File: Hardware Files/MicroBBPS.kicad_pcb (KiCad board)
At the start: 2 copper layers, 54 x 100 mm, 24 parts, among them J1 Conn_01x06, J2 USB_B_Micro, J3 Conn_02x03_Counter_Clockwise, J4 Conn_02x03_Counter_Clockwise, J5 Conn_01x02, J8 3PoleHeaderSwitch, J9 3PoleHeaderSwitch, U1 NCP1117ST50T3G, U3 NCP1117ST33T3G

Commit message: Update routing to match main
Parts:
- removed J1: Conn_01x06, MicroBBPS:Breadboard_Row_25
- removed REF** (x2): MountingHole_3.2mm_M3_ISO7380, MountingHole:MountingHole_3.2mm_M3_ISO7380
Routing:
- net /VoutRight: track 78.2 -> 0.00 mm
- net /VoutLeft: track 75.1 -> 0.00 mm
- net VS: track 42.7 -> 53.7 mm, vias 1 -> 3
- net GND: vias 0 -> 4
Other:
- board size 54 x 100 mm -> 54 x 23 mm

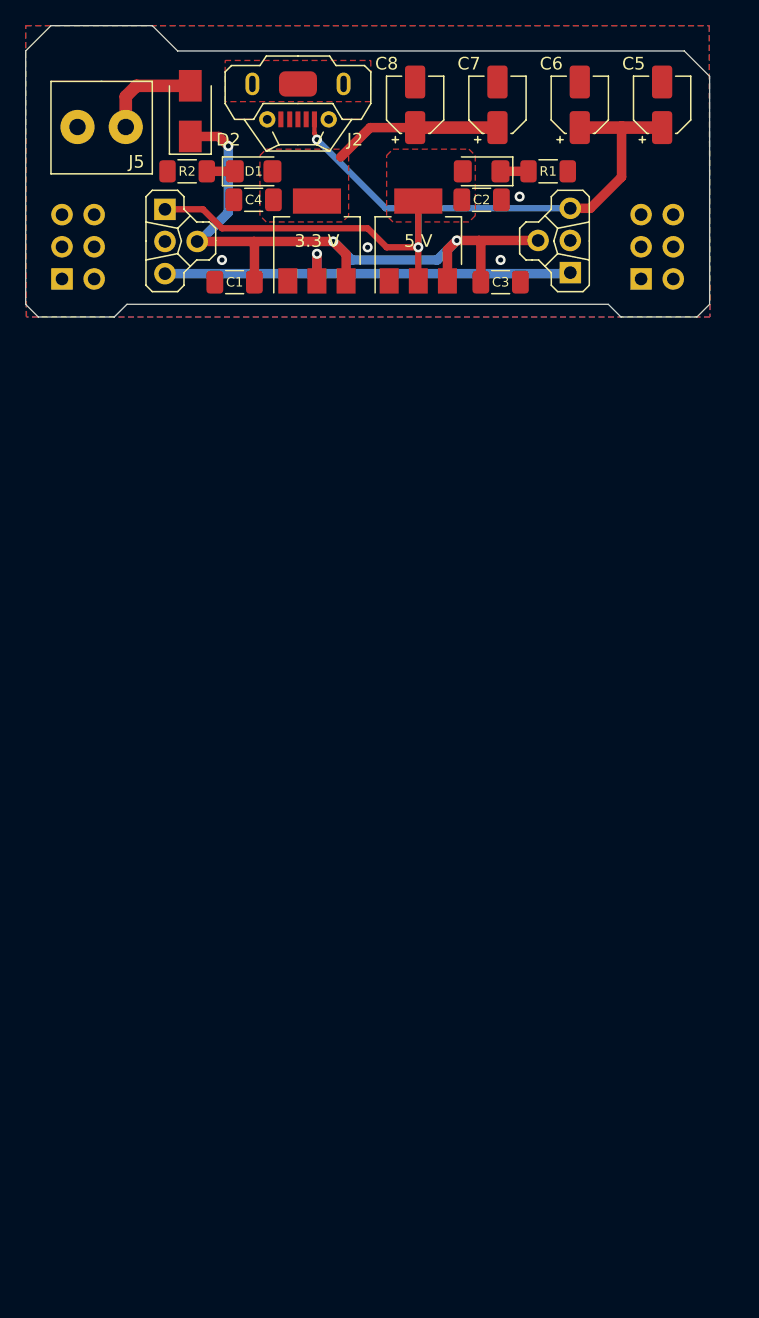
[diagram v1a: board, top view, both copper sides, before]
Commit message: Fix board version mismatch
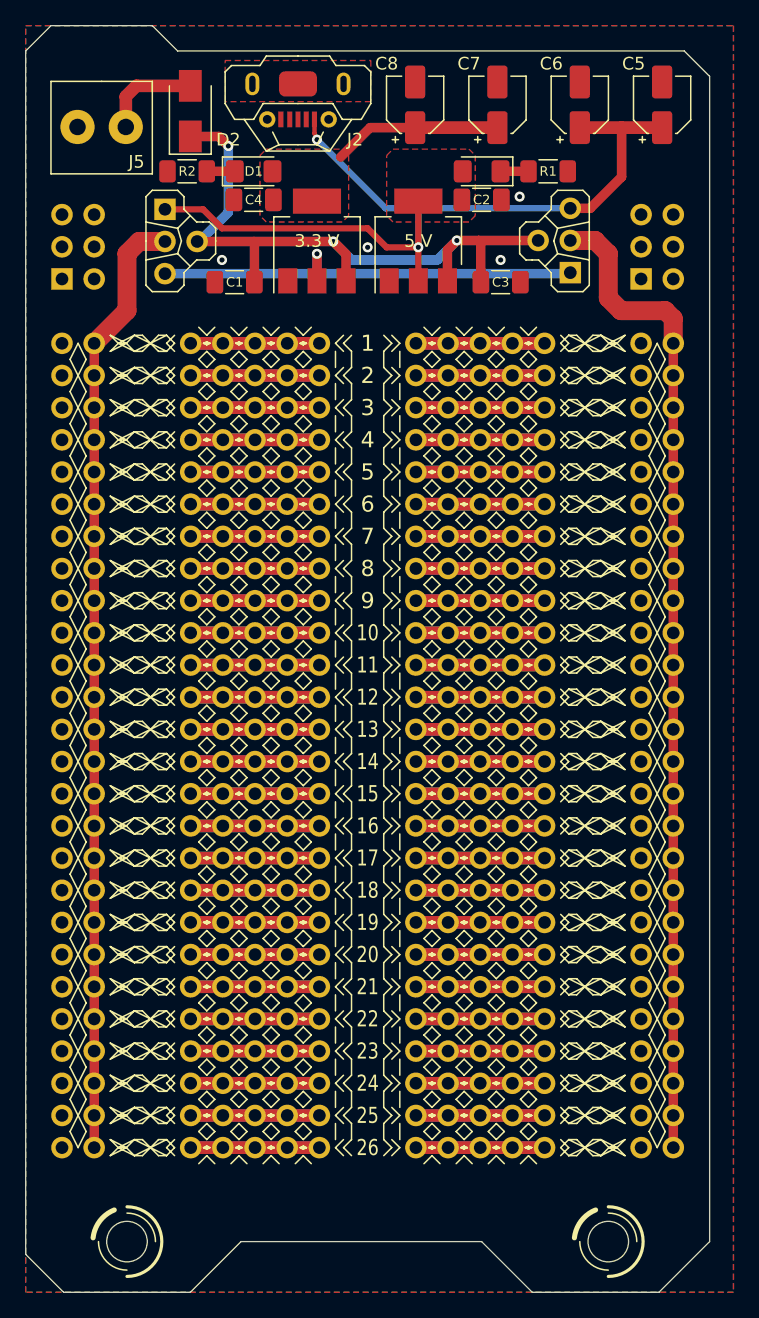
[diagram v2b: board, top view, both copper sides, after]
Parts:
- added J1: Conn_01x06, MicroBBPS:Breadboard_Row_25, F.Cu at (27.0, 25.1)
- added REF**: MountingHole_3.2mm_M3_ISO7380, MountingHole:MountingHole_3.2mm_M3_ISO7380, F.Cu at (8.00, 96.0)
- added REF**: MountingHole_3.2mm_M3_ISO7380, MountingHole:MountingHole_3.2mm_M3_ISO7380, F.Cu at (46.0, 96.0)
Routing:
- net /VoutRight: track 0.00 -> 78.2 mm
- net /VoutLeft: track 0.00 -> 75.1 mm
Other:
- board size 54 x 23 mm -> 54 x 100 mm

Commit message: Match main version
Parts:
- removed J3, J4: Conn_02x03_Counter_Clockwise, Connector_PinHeader_2.54mm:PinHeader_2x03_P2.54mm_Vertical
- added REF**: MountingHole_3.2mm_M3_ISO7380, MountingHole:MountingHole_3.2mm_M3_ISO7380, F.Cu at (49.0, 16.0)
- added REF**: MountingHole_3.2mm_M3_ISO7380, MountingHole:MountingHole_3.2mm_M3_ISO7380, F.Cu at (5.00, 16.0)
- moved REF** 3.00 mm to (5.00, 96.0)
- moved REF** 3.00 mm to (49.0, 96.0)

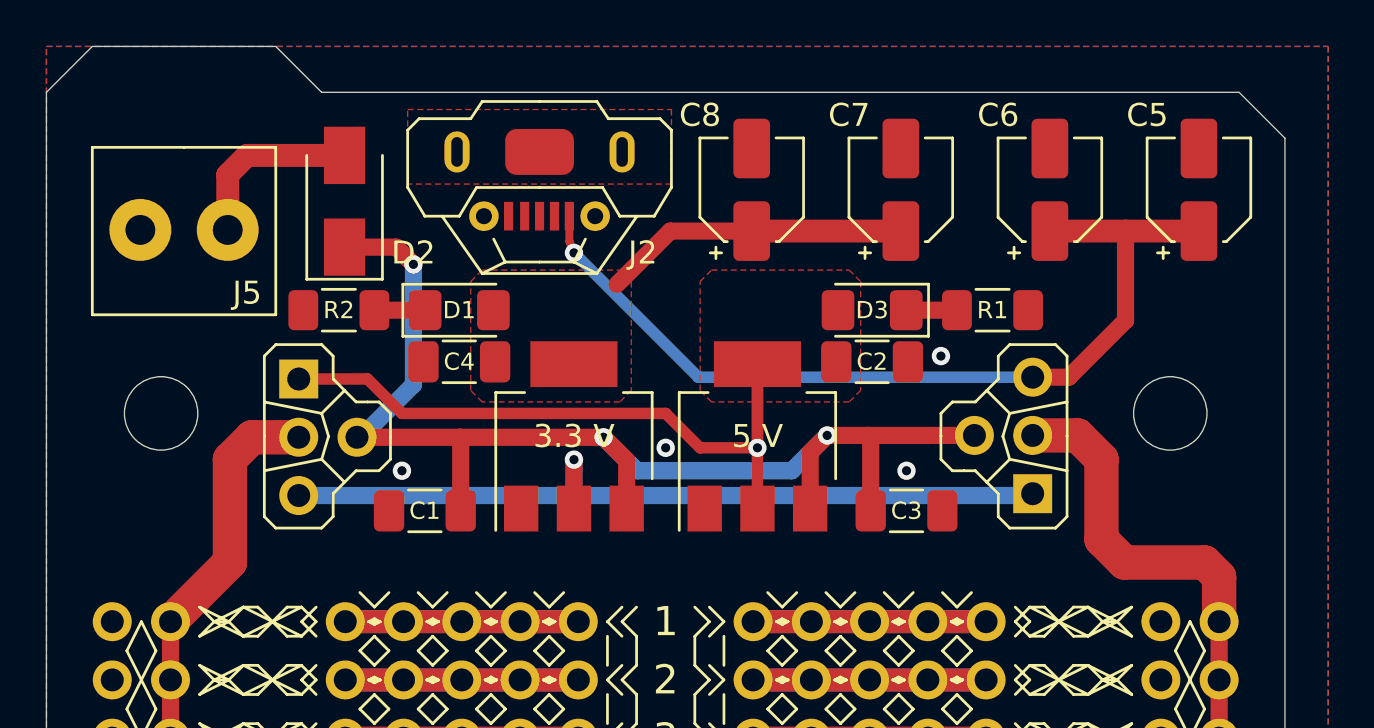
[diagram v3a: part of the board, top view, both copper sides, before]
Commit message: update D2 Position
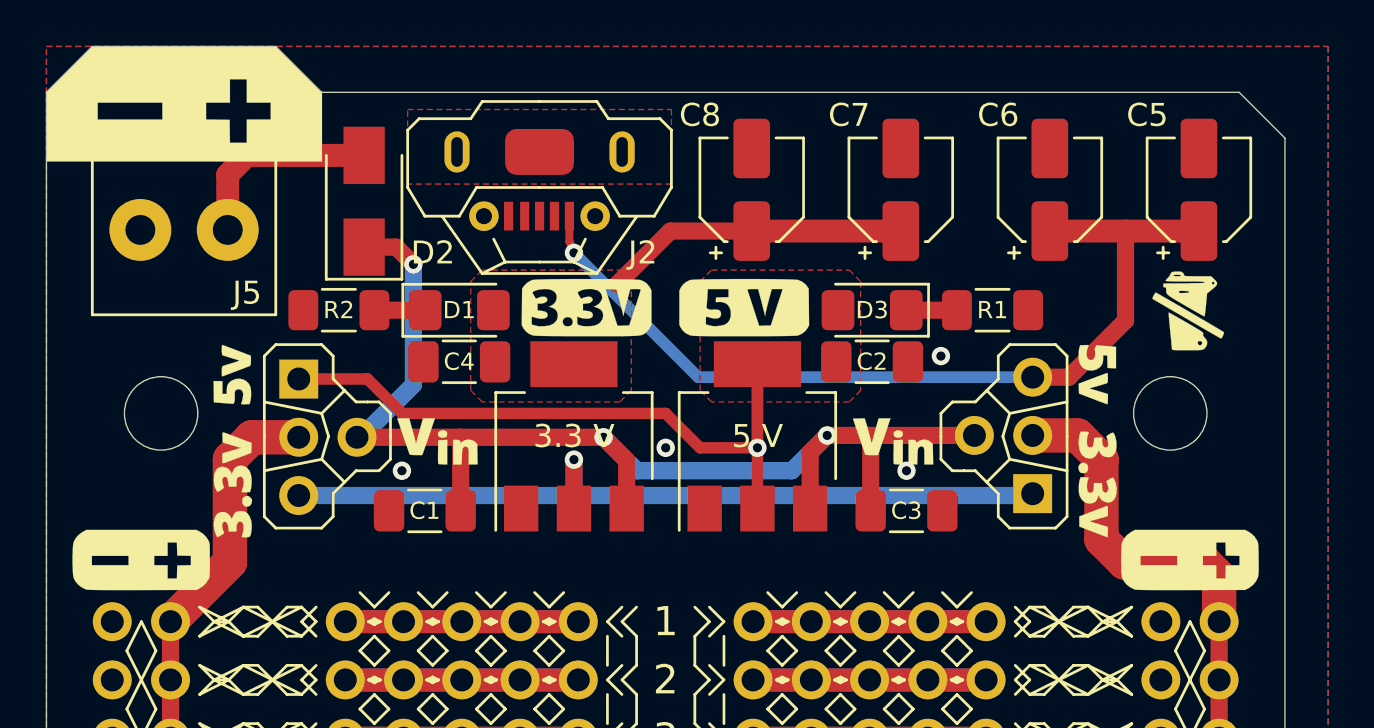
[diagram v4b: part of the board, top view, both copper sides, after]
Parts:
- added G***: LOGO, MicroBBPS:artwork-bottom, B.Cu at (27.0, 12.0)
- added G***: LOGO, MicroBBPS:artwork-top, F.Cu at (27.0, 12.0)
- moved D2 0.85 mm to (13.8, 6.75)
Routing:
- net VS: track 53.7 -> 52.9 mm

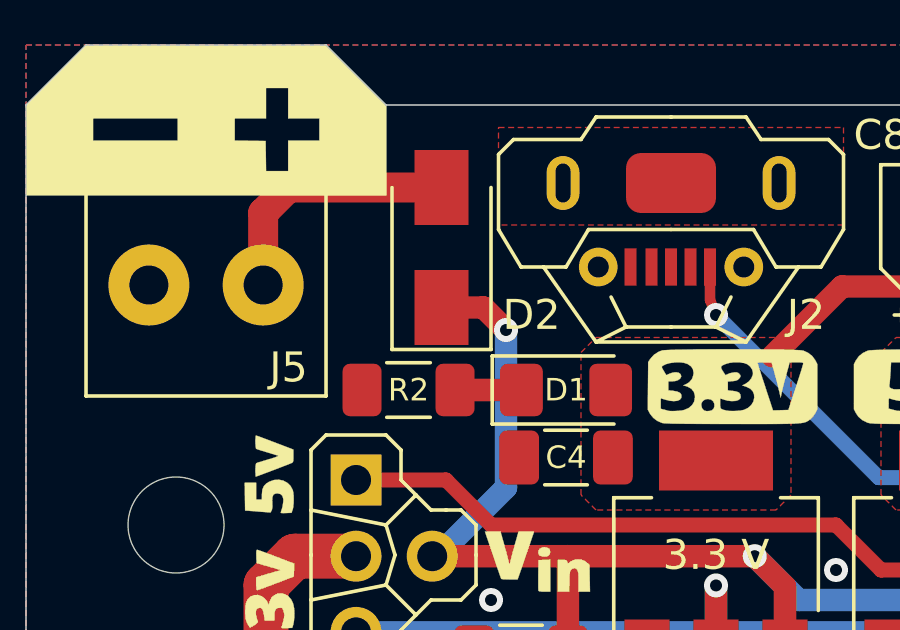
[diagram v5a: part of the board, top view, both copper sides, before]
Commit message: add details to Breadboard_Row_25.kicad_mod details
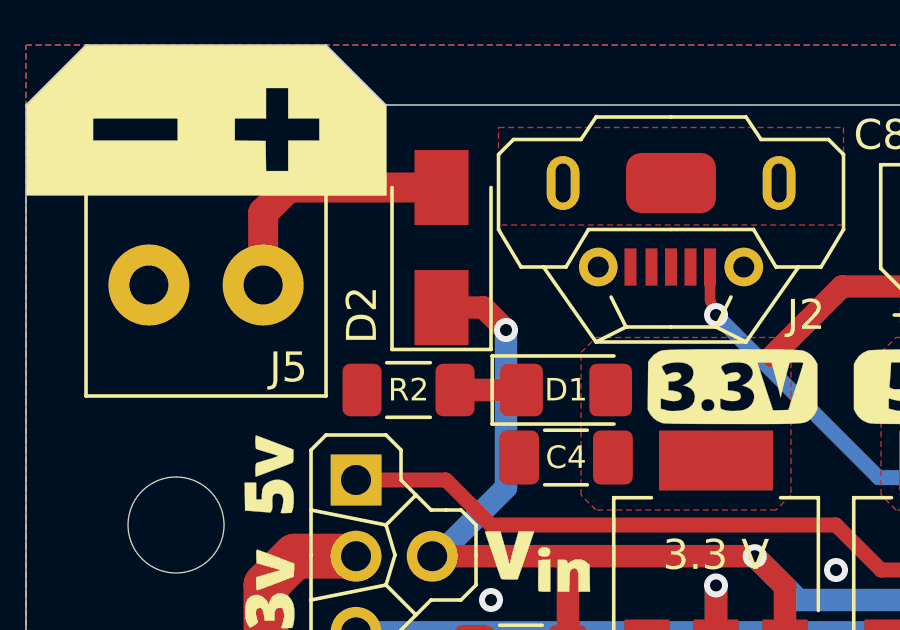
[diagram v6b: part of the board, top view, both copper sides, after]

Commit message: Finalize artwork
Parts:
- added G***: LOGO, MicroBBPS:artwork-plusminus, B.Cu at (27.0, 91.2)
- added G***: LOGO, MicroBBPS:artwork-plusminus, F.Cu at (27.0, 91.2)
- added G***: LOGO, MicroBBPS:artwork-plusminus, B.Cu at (27.0, 22.4)
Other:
- outline, holes or cut-outs redrawn
